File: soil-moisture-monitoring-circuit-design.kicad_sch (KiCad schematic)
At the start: 9 parts, among them J1 Conn_01x05_Analog_Soil_moistu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, J3 Conn_01x04_I2C_Soil_moisture, U1 DPT_Walter, U2 904, U3 904, U4 2465, U5 254, U6 BME680

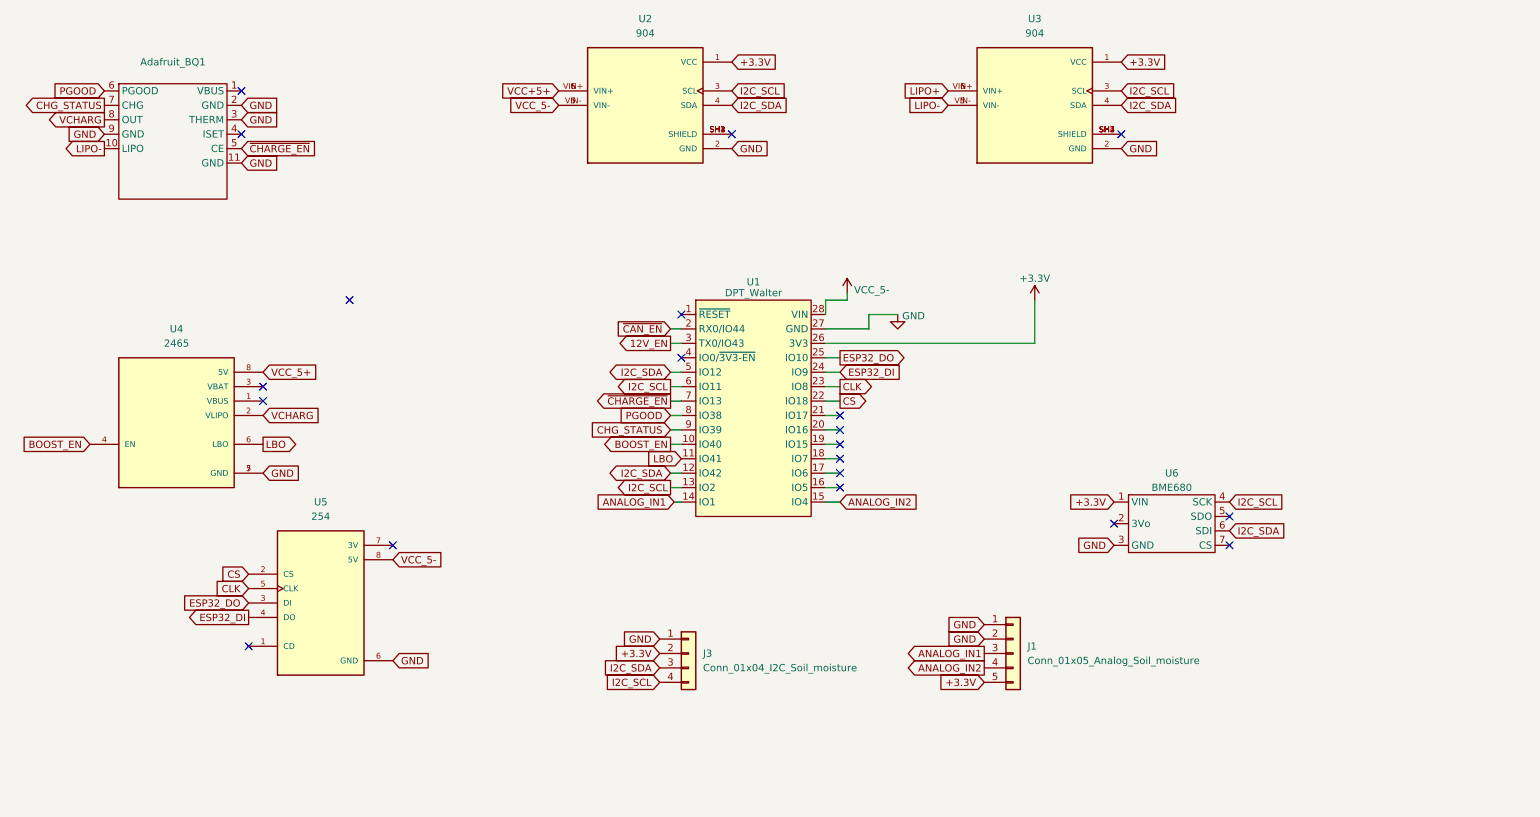
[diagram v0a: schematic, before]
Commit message: Initial placement and routing
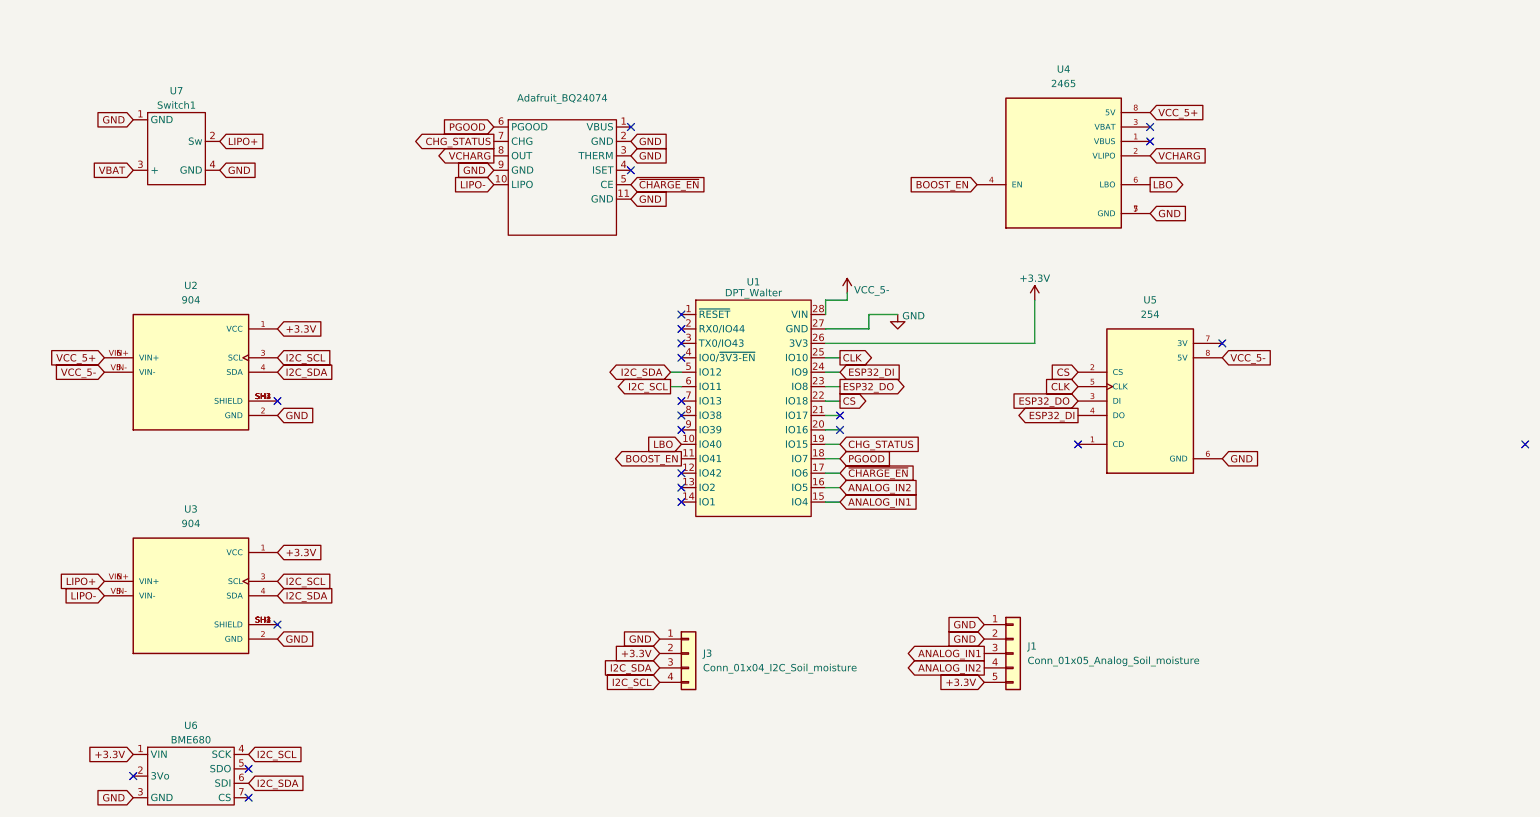
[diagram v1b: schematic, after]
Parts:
- added U7: Switch1, symbol adafruit_custom:Adafruit_JST_Switch
- J3: footprint Connector_PinHeader_2.54mm:PinHeader_1x04_P2.54mm_Vertical -> Connector_PinHeader_2.00mm:PinHeader_1x04_P2.00mm_Vertical
- renumbered Adafruit_BQ1 to Adafruit_BQ24074
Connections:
- net VCC+5+ is gone; now on net VCC_5+: U2.6 (VIN+), U2.VIN+
- net ANALOG_IN1: now also U1.15 (IO4); no longer U1.14 (IO1)
- net ANALOG_IN2: now also U1.16 (IO5); no longer U1.15 (IO4)
- net BOOST_EN: now also U1.11 (IO41); no longer U1.10 (IO40)
- net CHG_STATUS: now also U1.19 (IO15); no longer U1.9 (IO39)
- net CLK: now also U1.25 (IO10); no longer U1.23 (IO8)
- net ESP32_DO: now also U1.23 (IO8); no longer U1.25 (IO10)
- net GND: now also U7.1 (GND), U7.4 (GND)
- net I2C_SCL: no longer U1.13 (IO2)
- net I2C_SDA: no longer U1.12 (IO42)
- net LBO: now also U1.10 (IO40); no longer U1.11 (IO41)
- net LIPO+: now also U7.2 (Sw)
- net PGOOD: now also U1.18 (IO7); no longer U1.8 (IO38)
- net ~{CHARGE_EN}: now also U1.17 (IO6); no longer U1.7 (IO13)
- net 12V_EN: no longer names the net of U1.3 (TX0/IO43)
- net ~{CAN_EN}: no longer names the net of U1.2 (RX0/IO44)
- new net VBAT: U7.3 (+)
- no-connect marks 20 -> 24
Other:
- moved on the sheet: Adafruit_BQ24074, U2, U3, U4, U5, U6

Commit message: updated simplified design from Karun Potty
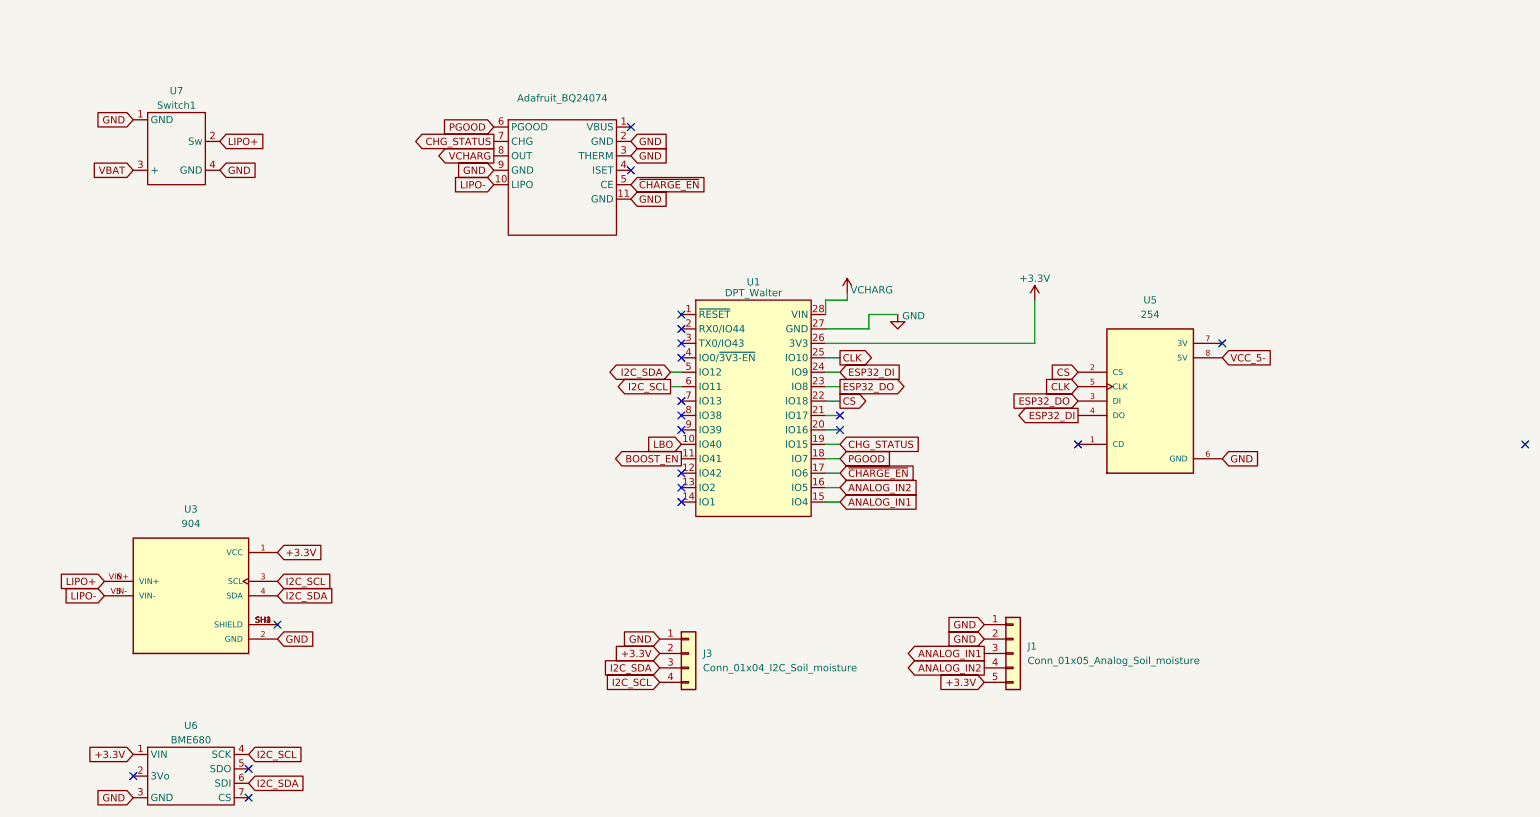
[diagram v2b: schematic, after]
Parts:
- removed U2: 904, Adafruit_INA219:MODULE_904, symbol Adafruit_INA219:904
- removed U4: 2465, Adafruit_Powerboost1000:MODULE_2465, symbol Adafruit_Powerboost1000:2465
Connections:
- net VCC_5-: no longer U1.28 (VIN)
- net VCHARG: now also U1.28 (VIN)
- no-connect marks 24 -> 21
